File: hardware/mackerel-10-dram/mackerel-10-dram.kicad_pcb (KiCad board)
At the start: 4 copper layers, 150 x 80 mm, 28 parts, among them J1 Conn_02x20_Odd_Even, J2 Conn_02x20_Odd_Even, J3 Conn_02x05_Odd_Even, U4 74HC245, U5 74HC245

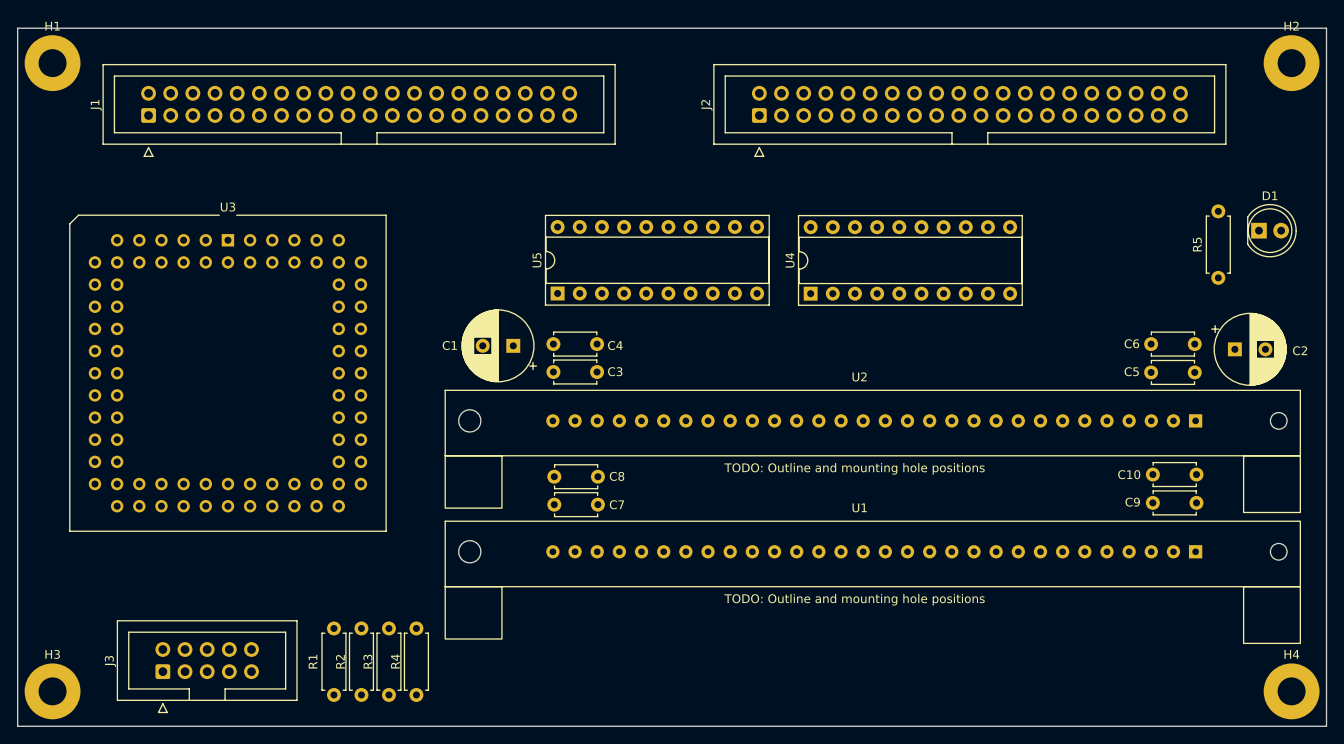
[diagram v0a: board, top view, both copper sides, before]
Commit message: Cleaned up the DRAM verilog and routed most of the PCB
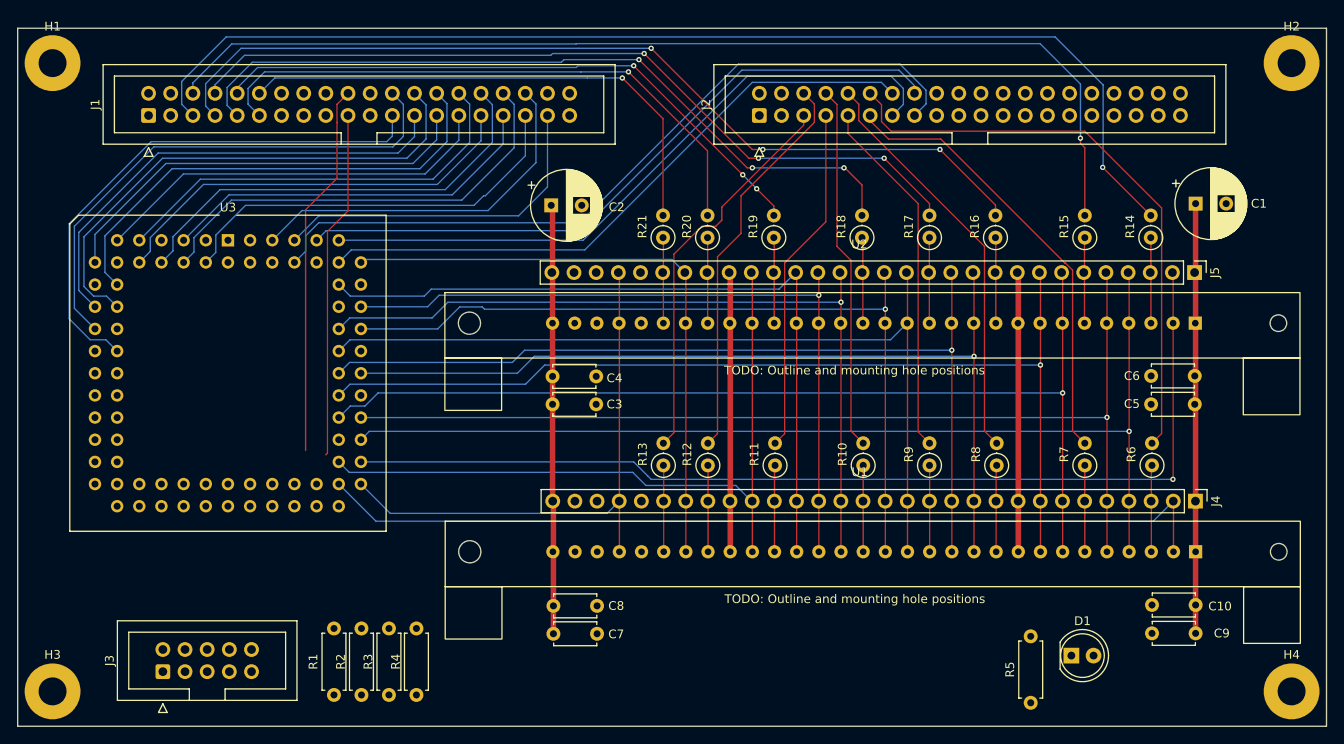
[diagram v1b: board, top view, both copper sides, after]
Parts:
- removed U4, U5: 74HC245, Package_DIP:DIP-20_W7.62mm_Socket
- added J4: Conn_01x30, Connector_PinHeader_2.54mm:PinHeader_1x30_P2.54mm_Vertical, F.Cu at (155.0, 74.2)
- added J5: Conn_01x30, Connector_PinHeader_2.54mm:PinHeader_1x30_P2.54mm_Vertical, F.Cu at (154.9, 48.0)
- added R10: 22, Resistor_THT:R_Axial_DIN0207_L6.3mm_D2.5mm_P2.54mm_Vertical, F.Cu at (116.9, 70.1)
- added R11: 22, Resistor_THT:R_Axial_DIN0207_L6.3mm_D2.5mm_P2.54mm_Vertical, F.Cu at (106.8, 70.1)
- added R12: 22, Resistor_THT:R_Axial_DIN0207_L6.3mm_D2.5mm_P2.54mm_Vertical, F.Cu at (99.1, 70.1)
- added R13: 22, Resistor_THT:R_Axial_DIN0207_L6.3mm_D2.5mm_P2.54mm_Vertical, F.Cu at (94.0, 70.1)
- added R14: 22, Resistor_THT:R_Axial_DIN0207_L6.3mm_D2.5mm_P2.54mm_Vertical, F.Cu at (149.9, 44.0)
- added R15: 22, Resistor_THT:R_Axial_DIN0207_L6.3mm_D2.5mm_P2.54mm_Vertical, F.Cu at (142.3, 44.0)
- added R16: 22, Resistor_THT:R_Axial_DIN0207_L6.3mm_D2.5mm_P2.54mm_Vertical, F.Cu at (132.1, 44.0)
- added R17: 22, Resistor_THT:R_Axial_DIN0207_L6.3mm_D2.5mm_P2.54mm_Vertical, F.Cu at (124.5, 44.0)
- added R18: 22, Resistor_THT:R_Axial_DIN0207_L6.3mm_D2.5mm_P2.54mm_Vertical, F.Cu at (116.8, 44.0)
- added R19: 22, Resistor_THT:R_Axial_DIN0207_L6.3mm_D2.5mm_P2.54mm_Vertical, F.Cu at (106.7, 44.0)
- added R20: 22, Resistor_THT:R_Axial_DIN0207_L6.3mm_D2.5mm_P2.54mm_Vertical, F.Cu at (99.1, 44.0)
- added R21: 22, Resistor_THT:R_Axial_DIN0207_L6.3mm_D2.5mm_P2.54mm_Vertical, F.Cu at (94.0, 44.0)
- added R6: 22, Resistor_THT:R_Axial_DIN0207_L6.3mm_D2.5mm_P2.54mm_Vertical, F.Cu at (150.0, 70.1)
- added R7: 22, Resistor_THT:R_Axial_DIN0207_L6.3mm_D2.5mm_P2.54mm_Vertical, F.Cu at (142.3, 70.1)
- added R8: 22, Resistor_THT:R_Axial_DIN0207_L6.3mm_D2.5mm_P2.54mm_Vertical, F.Cu at (132.2, 70.1)
- added R9: 22, Resistor_THT:R_Axial_DIN0207_L6.3mm_D2.5mm_P2.54mm_Vertical, F.Cu at (124.5, 70.1)
- moved C2 80.1 mm to (81.1, 40.3)
- moved C1 79.9 mm to (155.0, 40.1), turned to 0 degrees
- moved D1 53.2 mm to (140.8, 91.9)
- moved R5 53.2 mm to (136.1, 97.3)
- moved C10 15.0 mm to (155.0, 86.1)
- moved C9 15.0 mm to (155.0, 89.3)
- moved C7 14.8 mm to (81.4, 89.4)
- moved C8 14.8 mm to (81.4, 86.2)
- moved U2 11.2 mm to (155.0, 53.8)
- moved C3 3.70 mm to (81.3, 63.1)
- moved C4 3.70 mm to (81.3, 59.9)
- moved C5 3.65 mm to (154.9, 63.1)
- moved C6 3.65 mm to (154.9, 59.9)
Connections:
- U1 pad 10: RD5 -> RAM_D2
- U1 pad 13: RD4 -> RAM_D3
- U1 pad 16: RD3 -> RAM_D4
- U1 pad 20: RD2 -> RAM_D5
- U1 pad 23: RD1 -> RAM_D6
- U1 pad 25: RD0 -> RAM_D7
- U1 pad 3: RD7 -> RAM_D0
- U1 pad 6: RD6 -> RAM_D1
- U2 pad 10: RD10 -> RAM_D10
- U2 pad 13: RD11 -> RAM_D11
- U2 pad 16: RD12 -> RAM_D12
- U2 pad 20: RD13 -> RAM_D13
- U2 pad 23: RD14 -> RAM_D14
- U2 pad 25: RD15 -> RAM_D15
- U2 pad 3: RD8 -> RAM_D8
- U2 pad 6: RD9 -> RAM_D9
- U3 pad 10: A6 -> A13
- U3 pad 11: A7 -> A11
- U3 pad 12: A8 -> A9
- U3 pad 15: A9 -> A10
- U3 pad 16: A10 -> A21
- U3 pad 17: A11 -> A20
- U3 pad 18: A12 -> A22
- U3 pad 2: CLK_CPU -> GND
- U3 pad 20: A13 -> unconnected-(U3-IO-Pad20)
- U3 pad 21: unconnected-(U3-IO-Pad21) -> A23
- U3 pad 22: RAMWR -> unconnected-(U3-IO-Pad22)
- U3 pad 24: CAS0 -> unconnected-(U3-IO-Pad24)
- U3 pad 25: CAS1 -> unconnected-(U3-IO-Pad25)
- U3 pad 27: RAS -> unconnected-(U3-IO-Pad27)
- U3 pad 28: RAM_OE0 -> unconnected-(U3-IO-Pad28)
- U3 pad 29: RAM_OE1 -> unconnected-(U3-IO-Pad29)
- U3 pad 4: A1 -> A17
- U3 pad 5: A2 -> A15
- U3 pad 54: unconnected-(U3-IO-Pad54) -> RAS
- U3 pad 55: unconnected-(U3-IO-Pad55) -> CAS0
- U3 pad 56: unconnected-(U3-IO-Pad56) -> CAS1
- U3 pad 57: unconnected-(U3-IO-Pad57) -> RAMWR
- U3 pad 58: unconnected-(U3-IO-Pad58) -> RAM_A0
- U3 pad 6: A3 -> A16
- U3 pad 60: unconnected-(U3-IO-Pad60) -> RAM_A1
- U3 pad 61: unconnected-(U3-IO-Pad61) -> RAM_A2
- U3 pad 63: unconnected-(U3-IO-Pad63) -> RAM_A3
- U3 pad 64: unconnected-(U3-IO-Pad64) -> RAM_A4
- U3 pad 65: unconnected-(U3-IO-Pad65) -> RAM_A5
- U3 pad 67: unconnected-(U3-IO-Pad67) -> RAM_A6
- U3 pad 68: unconnected-(U3-IO-Pad68) -> RAM_A7
- U3 pad 69: A14 -> RAM_A8
- U3 pad 70: A15 -> RAM_A9
- U3 pad 73: A16 -> RAM_A10
- U3 pad 74: A17 -> RAM_A11
- U3 pad 75: A18 -> /AS
- U3 pad 76: A19 -> R/W
- U3 pad 77: A20 -> /LDS
- U3 pad 79: A21 -> A19
- U3 pad 8: A4 -> A14
- U3 pad 80: A22 -> /UDS
- U3 pad 81: A23 -> A18
- U3 pad 9: A5 -> A12
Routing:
- net D8: track 0.00 -> 131.7 mm, vias 0 -> 1
- net D9: track 0.00 -> 122.0 mm, vias 0 -> 1
- net RAM_A0: track 0.00 -> 120.5 mm, vias 0 -> 1
- net CAS1: track 0.00 -> 117.6 mm, vias 0 -> 1
- net RAM_A1: track 0.00 -> 117.6 mm, vias 0 -> 1
- net RAM_A2: track 0.00 -> 116.2 mm, vias 0 -> 1
- net RAM_A3: track 0.00 -> 113.9 mm, vias 0 -> 1
- net D10: track 0.00 -> 104.9 mm, vias 0 -> 3
- net CAS0: track 0.00 -> 104.2 mm
- net RAM_A5: track 0.00 -> 103.4 mm, vias 0 -> 1
- net RAM_A4: track 0.00 -> 103.1 mm, vias 0 -> 1
- net +5V: track 0.00 -> 98.6 mm
- net RAM_A6: track 0.00 -> 98.5 mm
- net RAM_A7: track 0.00 -> 93.3 mm, vias 0 -> 1
- net D11: track 0.00 -> 92.8 mm, vias 0 -> 3
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- removed copper zone on In2.Cu, net +5V
- removed copper zone on In1.Cu, net GND
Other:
- copper layers 4 -> 2

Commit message: Update CPLD pin assignments for DRAM breakout PCB
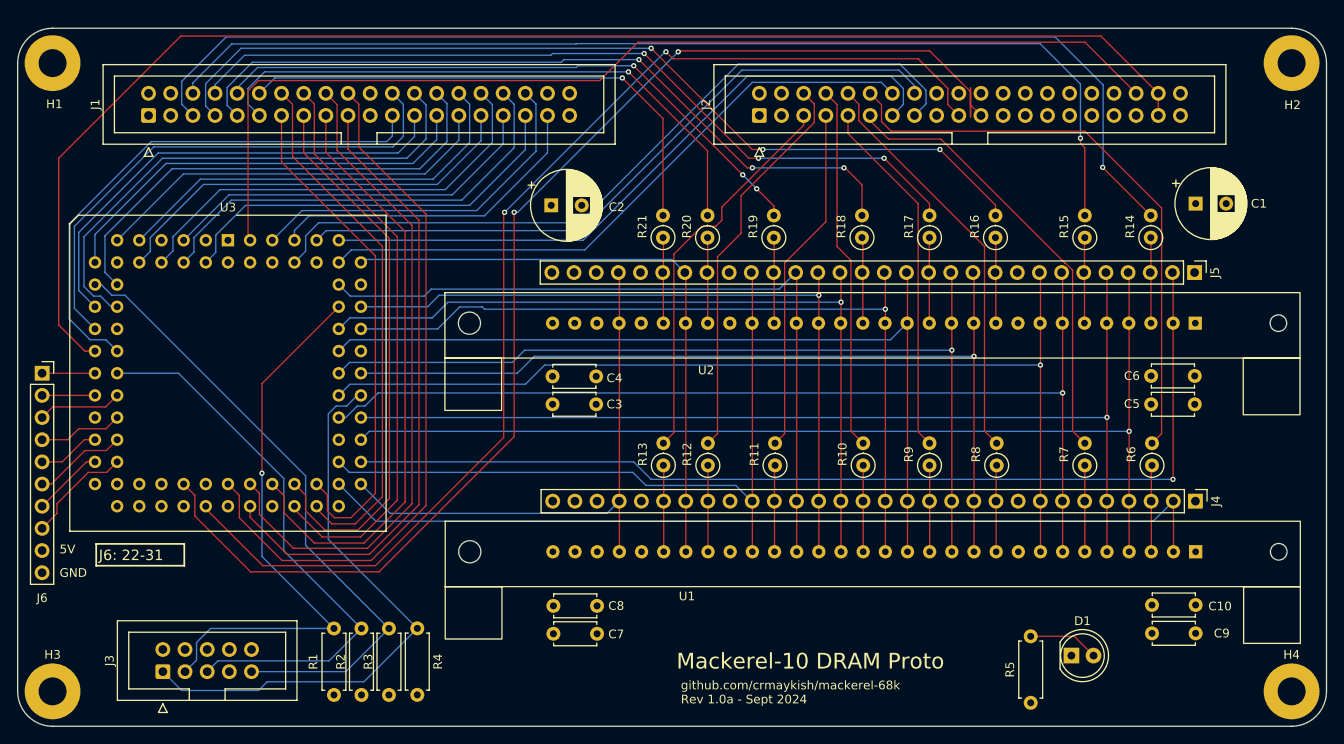
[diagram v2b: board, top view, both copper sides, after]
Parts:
- added J6: Conn_01x10, Connector_PinSocket_2.54mm:PinSocket_1x10_P2.54mm_Vertical, F.Cu at (22.8, 59.5)
- moved R4 7.63 mm to (65.8, 88.8), turned to -90 degrees
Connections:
- U3 pad 20: unconnected-(U3-IO-Pad20) -> /RESET
- U3 pad 22: unconnected-(U3-IO-Pad22) -> Net-(J6-Pin_1)
- U3 pad 24: unconnected-(U3-IO-Pad24) -> Net-(J6-Pin_2)
- U3 pad 25: unconnected-(U3-IO-Pad25) -> Net-(J6-Pin_3)
- U3 pad 27: unconnected-(U3-IO-Pad27) -> Net-(J6-Pin_4)
- U3 pad 28: unconnected-(U3-IO-Pad28) -> Net-(J6-Pin_5)
- U3 pad 29: unconnected-(U3-IO-Pad29) -> Net-(J6-Pin_6)
- U3 pad 30: unconnected-(U3-IO-Pad30) -> Net-(J6-Pin_7)
- U3 pad 31: unconnected-(U3-IO-Pad31) -> Net-(J6-Pin_8)
- U3 pad 40: unconnected-(U3-IO-Pad40) -> /DTACK_EXP
- U3 pad 41: unconnected-(U3-IO-Pad41) -> /EXP
- U3 pad 44: unconnected-(U3-IO-Pad44) -> A8
- U3 pad 45: unconnected-(U3-IO-Pad45) -> A7
- U3 pad 46: unconnected-(U3-IO-Pad46) -> A6
- U3 pad 48: unconnected-(U3-IO-Pad48) -> A5
- U3 pad 49: unconnected-(U3-IO-Pad49) -> A4
- U3 pad 50: unconnected-(U3-IO-Pad50) -> A3
- U3 pad 51: unconnected-(U3-IO-Pad51) -> A2
- U3 pad 52: unconnected-(U3-IO-Pad52) -> A1
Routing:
- net /RESET: track 0.00 -> 161.6 mm
- net /DTACK_EXP: track 0.00 -> 147.5 mm, vias 0 -> 2
- net /EXP: track 0.00 -> 132.8 mm, vias 0 -> 2
- net CLK_SRC: track 0.00 -> 123.7 mm
- net +5V: track 98.6 -> 0.00 mm
- net A6: track 0.00 -> 76.3 mm
- net TDI: track 0.00 -> 72.5 mm
- net A5: track 0.00 -> 69.2 mm
- net TCK: track 0.00 -> 66.4 mm
- net A4: track 0.00 -> 66.3 mm
- net TMS: track 0.00 -> 64.7 mm
- net TDO: track 0.00 -> 64.2 mm, vias 0 -> 1
- net A3: track 0.00 -> 63.6 mm
- net A2: track 0.00 -> 60.9 mm
- net A1: track 0.00 -> 58.3 mm
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- added copper zone on In2.Cu, net +5V
- added copper zone on In1.Cu, net GND
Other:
- outline, holes or cut-outs redrawn
- copper layers 2 -> 4
- board text added: "5V"
- board text added: "GND"
- board text added: "J6: 22-31"
- board text added: "Mackerel-10 DRAM Proto"
- board text added: "github.com/crmaykish/mackerel-68k Rev 1.0a - Sept 2024"
